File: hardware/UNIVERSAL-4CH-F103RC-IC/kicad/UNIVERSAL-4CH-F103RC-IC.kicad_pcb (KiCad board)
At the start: 2 copper layers, 136 x 105 mm, 142 parts, among them J1 ACTUATOR_CH1_4P, J2 ACTUATOR_CH2_4P, J201 REED_A_OPEN_3V3_SIG_GND, J202 REED_A_CLOSED_3V3_SIG_GND, J203 REED_A_IN_PLACE_3V3_SIG_GND, J211 CAP_CS1_GND, J212 CAP_CS2_GND, J213 CAP_CS3_GND, J220 SWD_S1_3V3_DIO_CLK_NRST_GND, J230 LOGIC_12V_GND, J240 CANH_CANL_GND_SHIELD, J280B WIRE_FROM_C280_POS, J3 ACTUATOR_CH3_4P, J4 ACTUATOR_CH4_4P, U1 VNH5019A-E, U2 VNH5019A-E, U230 AMS1117-3V3, U250 25LC256_SOIC8_CARRIER_ID, U270 TLV6700DDCR_POWER_MONITOR, U3 VNH5019A-E, U300 STM32F103RCT6, U4 VNH5019A-E, Y300 8MHz

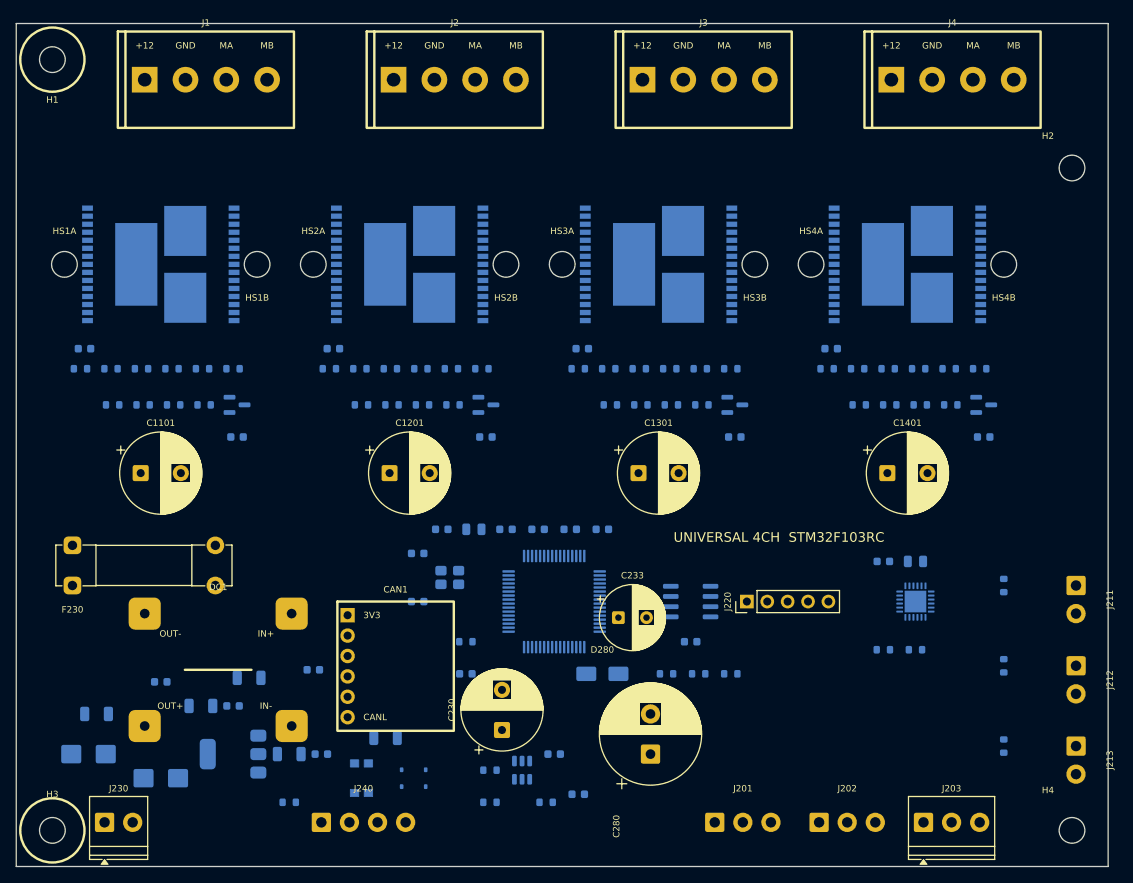
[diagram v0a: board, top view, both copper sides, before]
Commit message: hardware: save compact user 4-channel placement
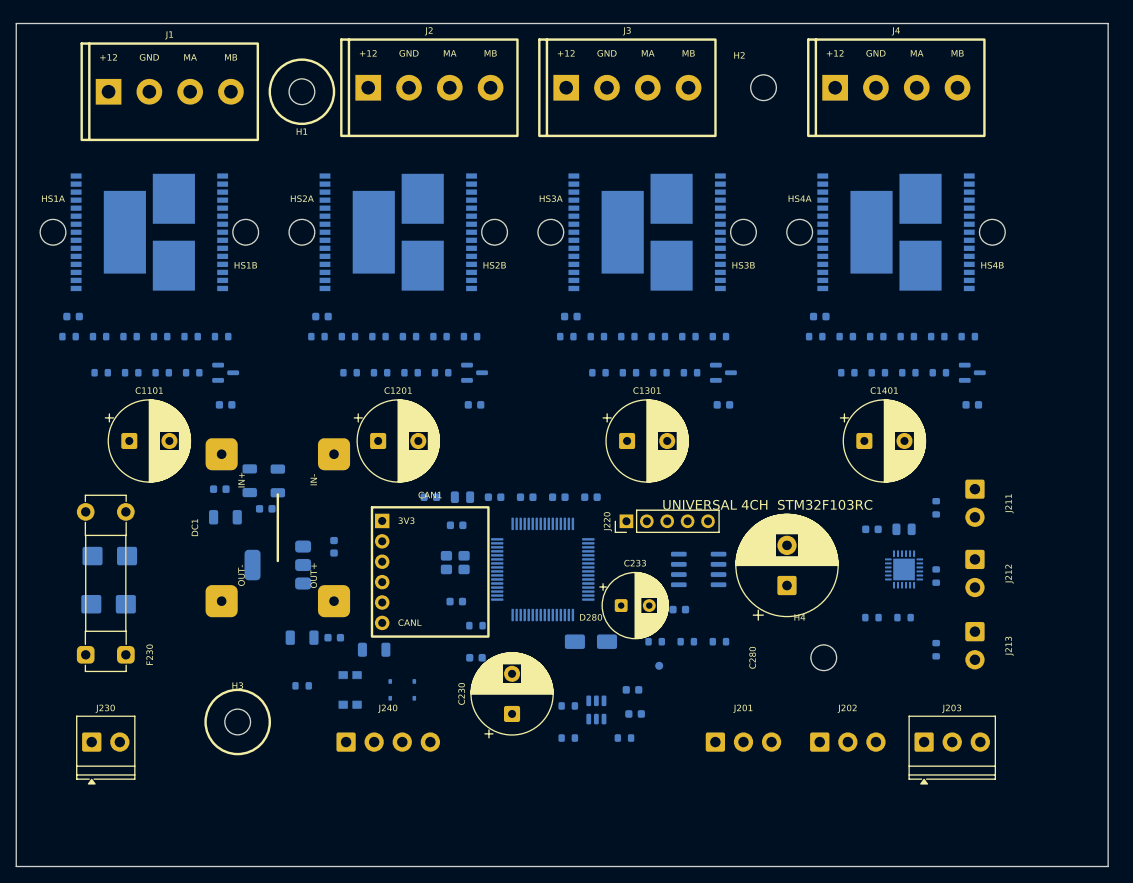
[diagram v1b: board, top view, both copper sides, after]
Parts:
- moved H2 39.7 mm to (93.1, 8.00)
- moved H4 37.7 mm to (100.6, 79.0)
- moved H1 31.3 mm to (35.6, 8.50)
- moved C231 29.3 mm to (26.1, 61.5)
- moved C234 28.7 mm to (29.1, 57.0), turned to 90 degrees
- moved C280 27.0 mm to (96.0, 70.0)
- moved H3 26.7 mm to (27.6, 87.0)
- moved C232 25.1 mm to (25.4, 58.0)
- moved C235 24.9 mm to (31.1, 60.5)
- moved D230 24.8 mm to (11.7, 66.3)
- moved C236 24.8 mm to (32.6, 57.0), turned to 90 degrees
- moved U230 24.2 mm to (32.6, 67.5)
- moved D231 22.6 mm to (11.5, 72.3), turned to 0 degrees
- moved J213 19.0 mm to (119.4, 75.8)
- moved J212 18.3 mm to (119.4, 66.8)
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
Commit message: hardware: trim compact 4-channel board to 124x93
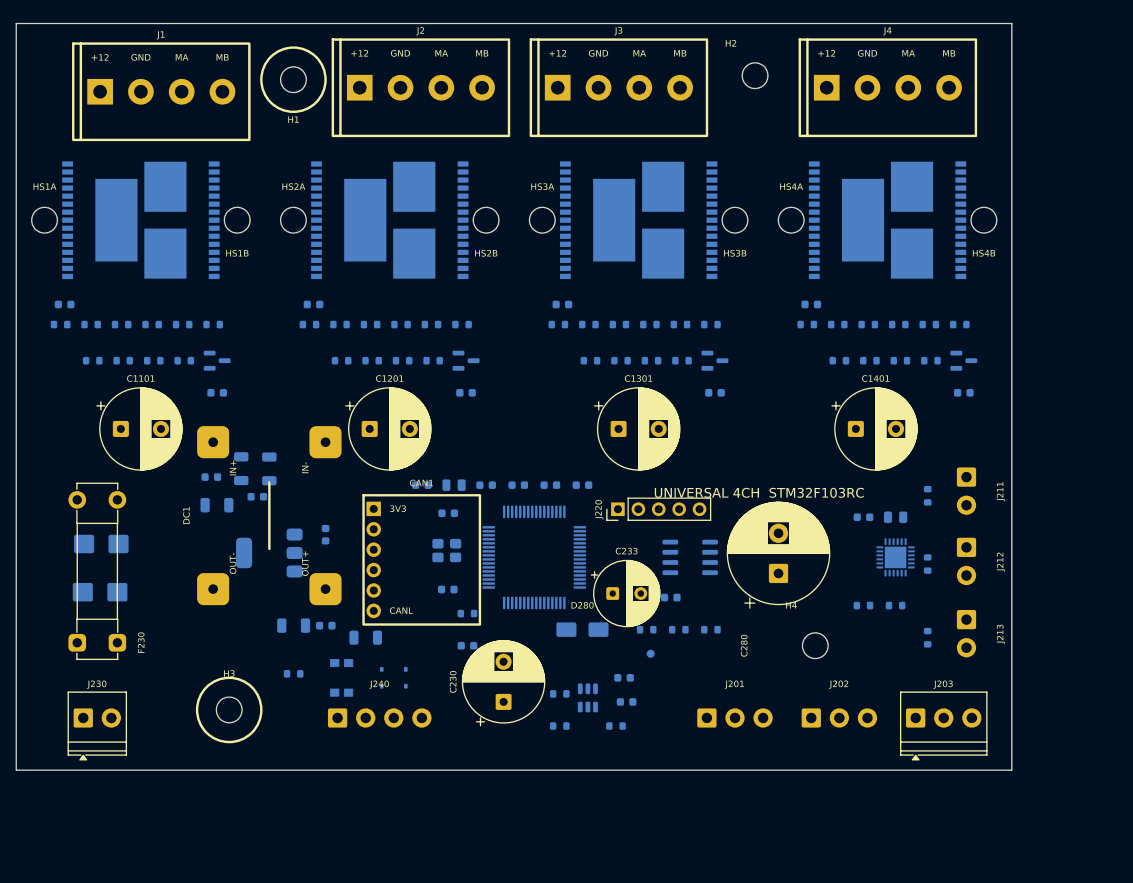
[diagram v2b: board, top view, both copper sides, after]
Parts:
- moved J230 3.18 mm to (8.35, 86.5)
- moved J240 3.18 mm to (40.0, 86.5)
- moved J201 3.18 mm to (86.0, 86.5)
- moved J202 3.18 mm to (99.0, 86.5)
- moved J203 3.18 mm to (112.0, 86.5)
- moved C280 1.83 mm to (94.9, 68.5)
- moved J220 1.83 mm to (74.9, 60.5)
- moved R1303 1.83 mm to (75.1, 37.5)
- moved R1304 1.83 mm to (78.9, 37.5)
- moved R1305 1.83 mm to (82.7, 37.5)
- moved R1309 1.83 mm to (79.1, 42.0)
- moved R1310 1.83 mm to (82.9, 42.0)
- moved R1403 1.83 mm to (106.1, 37.5)
- moved R1404 1.83 mm to (109.9, 37.5)
- moved R1405 1.83 mm to (113.7, 37.5)
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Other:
- board size 136 x 105 mm -> 124 x 93 mm

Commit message: Complete routed four-channel F103RC controller PCB
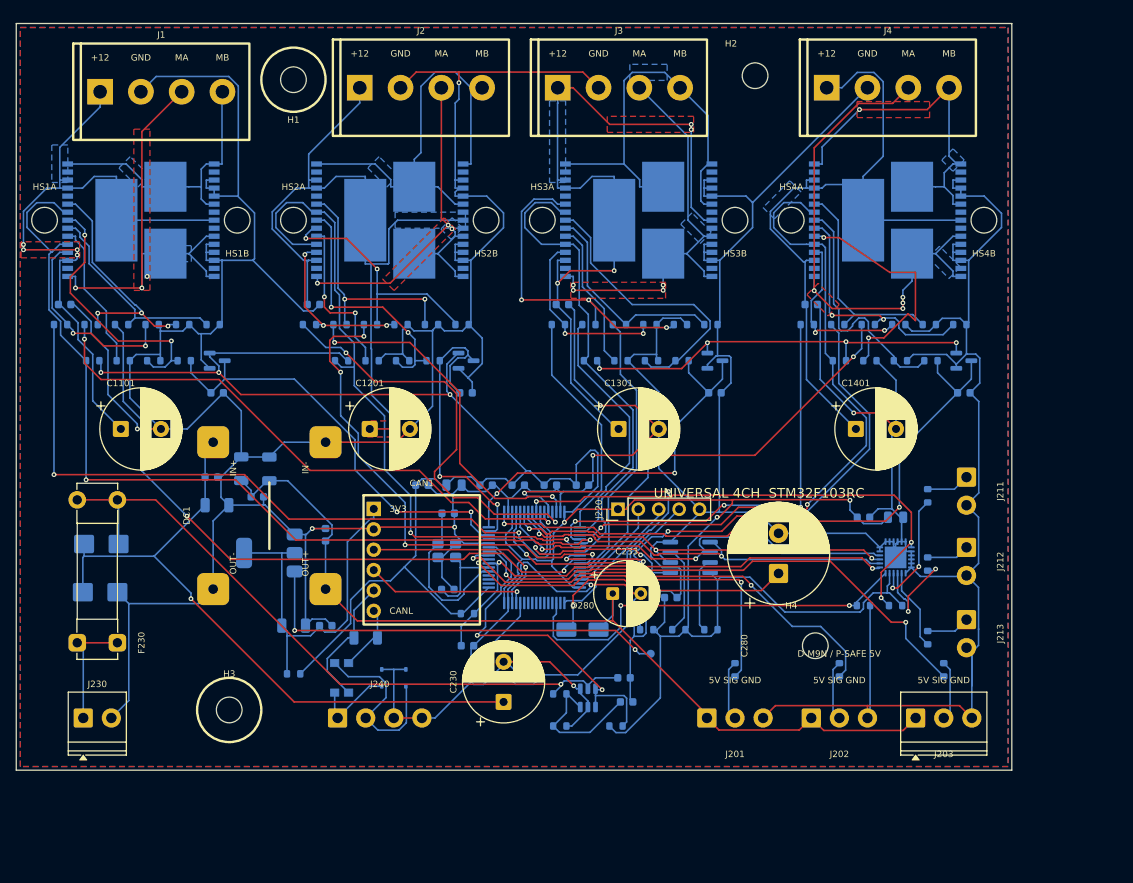
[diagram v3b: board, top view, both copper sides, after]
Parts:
- added R290: 4.7K 1% REED INPUT SERIES, R_0603_1608Metric, B.Cu at (89.5, 80.5)
- added R291: 4.7K 1% REED INPUT SERIES, R_0603_1608Metric, B.Cu at (102.5, 80.5)
- added R292: 4.7K 1% REED INPUT SERIES, R_0603_1608Metric, B.Cu at (115.5, 80.5)
- J201: value REED_A_OPEN_3V3_SIG_GND -> REED_A_OPEN_5V_SIG_GND_PROTECTED
- J202: value REED_A_CLOSED_3V3_SIG_GND -> REED_A_CLOSED_5V_SIG_GND_PROTECTED
- J203: value REED_A_IN_PLACE_3V3_SIG_GND -> REED_A_IN_PLACE_5V_SIG_GND_PROTECTED
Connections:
- J201 pad 1: S1_3V3 -> LOGIC_5V
- J201 pad 2: REED_A_OPEN -> REED_A_OPEN_RAW_5V
- J202 pad 1: S1_3V3 -> LOGIC_5V
- J202 pad 2: REED_A_CLOSED -> REED_A_CLOSED_RAW_5V
- J203 pad 1: S1_3V3 -> LOGIC_5V
- J203 pad 2: REED_A_IN_PLACE -> REED_A_IN_PLACE_RAW_5V
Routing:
- net GND: track 0.00 -> 946.5 mm, vias 0 -> 9
- net S1_3V3: track 0.00 -> 332.7 mm, vias 0 -> 6
- net LOGIC_5V: track 0.00 -> 115.6 mm
- net CH1_DIAG: track 0.00 -> 113.1 mm, vias 0 -> 2
- net FUSED_12V_CH3: track 0.00 -> 98.1 mm, vias 0 -> 4
- net FUSED_12V_CH2: track 0.00 -> 96.9 mm, vias 0 -> 2
- net CH1_INA_MCU: track 0.00 -> 91.0 mm, vias 0 -> 2
- net CH4_DIAG: track 0.00 -> 90.2 mm, vias 0 -> 4
- net FUSED_12V_CH4: track 0.00 -> 87.5 mm
- net FUSED_12V_CH1: track 0.00 -> 85.2 mm, vias 0 -> 4
- net LOGIC_12V_FUSED: track 0.00 -> 85.2 mm, vias 0 -> 1
- net CH2_DIAG: track 0.00 -> 84.0 mm, vias 0 -> 2
- net LOGIC_12V_PROTECTED: track 0.00 -> 83.5 mm, vias 0 -> 1
- net CH1_PWM_MCU: track 0.00 -> 80.8 mm, vias 0 -> 2
- net CH4_CURRENT_ADC: track 0.00 -> 79.9 mm, vias 0 -> 2
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- added copper zone on B.Cu, net CH1_OUTA
- added copper zone on F.Cu, net CH1_OUTA
- added copper zone on B.Cu, net CH1_OUTB
- added copper zone on B.Cu, net CH2_OUTA
- added copper zone on F.Cu, net CH2_OUTA
- added copper zone on B.Cu, net CH2_OUTB
- added copper zone on B.Cu, net CH3_OUTA
- added copper zone on F.Cu, net CH3_OUTA
- added copper zone on B.Cu, net CH3_OUTB
- added copper zone on B.Cu, net CH4_OUTA
- added copper zone on F.Cu, net CH4_OUTA
- added copper zone on B.Cu, net CH4_OUTB
- added copper zone on F.Cu, net CH4_OUTB
- added copper zone on B.Cu, net FUSED_12V_CH1
- added copper zone on F.Cu, net FUSED_12V_CH1
- added copper zone on B.Cu, net FUSED_12V_CH2
- added copper zone on F.Cu, net FUSED_12V_CH2
- added copper zone on B.Cu, net FUSED_12V_CH3
- added copper zone on F.Cu, net FUSED_12V_CH3
- added copper zone on B.Cu, net FUSED_12V_CH4
- added copper zone on B.Cu, net GND
- added copper zone on F.Cu, net GND
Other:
- board text added: "5V SIG GND"
- board text added: "C280+ -> J280B"
- board text added: "D-M9N / P-SAFE 5V"

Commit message: Fix universal 4ch power routing
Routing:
- net CH4_OUTA: track 66.8 -> 95.6 mm, vias 4 -> 10
- net CH3_OUTA: track 52.0 -> 80.7 mm, vias 4 -> 8
- net FUSED_12V_CH3: vias 4 -> 3
- net FUSED_12V_CH2: vias 2 -> 1
- net FUSED_12V_CH1: vias 4 -> 2
- removed copper zone on F.Cu, net CH4_OUTB
- removed copper zone on F.Cu, net FUSED_12V_CH1
- removed copper zone on F.Cu, net FUSED_12V_CH2
- removed copper zone on F.Cu, net FUSED_12V_CH3
